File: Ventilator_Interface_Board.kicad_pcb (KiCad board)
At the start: 2 copper layers, 60 x 88.5 mm, 53 parts, among them J1 ROTARY CONTROLS, J3 ALARM, J4 LCD DISPLAY, J5 OPTICAL SWITCH, J6 HOME LIMIT SWITCH, P1 Power, P2 Analog, P3 Digital, P4 Digital, P5 CONN_01X01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

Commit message: Rev A - pre-release
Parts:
- removed J5: OPTICAL SWITCH, Ventilator:Molex_KK-254_1x05_P2.54mm_Horizontal
- removed J6: HOME LIMIT SWITCH, Ventilator:Molex_KK-254_1x06_P2.54mm_Horizontal
- removed REF**: KiCad-Logo2_6mm_SilkScreen, Symbol:KiCad-Logo2_6mm_SilkScreen
- removed REF**: OSHW-Logo2_14.6x12mm_SilkScreen, Symbol:OSHW-Logo2_14.6x12mm_SilkScreen
- removed U2: HSCDRRN100MDAA5, Ventilator:DIP-8_W13.08mm
- added C7: 1uF, Capacitor_SMD:C_0603_1608Metric, F.Cu at (155.3, 111.8)
- added C8: 470pF, Capacitor_SMD:C_0603_1608Metric, F.Cu at (160.7, 104.9)
- added J2: Conn_01x08, Ventilator:PhoenixContact_PTSA_1,5_8-3_5-Z_1x08_P3.50mm_Vertical, F.Cu at (149.3, 68.4)
- added R10: 330R, Resistor_SMD:R_0603_1608Metric, F.Cu at (157.0, 128.6)
- added R9: 10K, Resistor_SMD:R_0603_1608Metric, F.Cu at (151.0, 127.6)
- J1: value ROTARY CONTROLS -> Conn_01x08; footprint Ventilator:Molex_KK-254_1x08_P2.54mm_Horizontal -> Ventilator:PhoenixContact_PTSA_1,5_8-3_5-Z_1x08_P3.50mm_Vertical
- J3: value ALARM -> Conn_01x08; footprint Ventilator:Molex_KK-254_1x04_P2.54mm_Horizontal -> Ventilator:PhoenixContact_PTSA_1,5_8-3_5-Z_1x08_P3.50mm_Vertical
- J4: value LCD DISPLAY -> Conn_01x08; footprint Ventilator:Molex_KK-254_1x12_P2.54mm_Horizontal -> Ventilator:PhoenixContact_PTSA_1,5_8-3_5-Z_1x08_P3.50mm_Vertical
- R3: value 10K -> DNF
- R7: value 330R -> 0R
- U1: value HSCMRRN100MDAA5 -> MP3V5004GP; footprint Ventilator:SMT-8W_7.5x8.8mm_P2.54mm -> Ventilator:SOP_16.8x7.62mm_P2.54mm
- moved J4 82.5 mm to (126.3, 132.5), turned to 0 degrees
- moved J1 64.9 mm to (180.3, 68.4), turned to 180 degrees
- moved J3 64.0 mm to (157.1, 132.5), turned to 0 degrees
- moved R2 22.0 mm to (133.3, 127.6), turned to 90 degrees
- moved R4 21.6 mm to (130.3, 127.6), turned to 90 degrees
- moved R3 20.6 mm to (151.6, 111.7)
- moved C5 20.4 mm to (179.1, 128.5), turned to 180 degrees
- moved R5 15.7 mm to (147.4, 127.6), turned to 90 degrees
- moved R7 15.1 mm to (149.6, 111.7), turned to 270 degrees
- moved C2 13.0 mm to (136.1, 127.5), turned to 270 degrees
- moved R8 9.56 mm to (139.6, 128.1), turned to 180 degrees
- moved C4 3.89 mm to (155.3, 110.0), turned to 180 degrees
- moved R1 3.01 mm to (133.9, 72.4), turned to 0 degrees
- moved R6 0.69 mm to (152.4, 72.7), turned to 0 degrees
- moved U1 0.30 mm to (155.3, 98.7)
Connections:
- C4 pad 2: +5V -> Net-(C4-Pad2)
- J1 pad 1: +5V -> GND
- J1 pad 2: /TIDAL_VOLUME -> +5V
- J1 pad 3: /BPM -> +5V
- J1 pad 4: /IF_RATE -> /LCD_RS
- J1 pad 5: /MAX_PRESSURE -> GND
- J1 pad 6: GND -> /LCD_EN
- J1 pad 7: (no net) -> /LCD_D4
- J1 pad 8: (no net) -> /LCD_D5
- J3 pad 1: /BUZZER_LED -> Net-(J3-Pad1)
- J3 pad 2: GND -> +5V
- J3 pad 3: /BUZZER_LED -> /TIDAL_VOLUME
- J3 pad 4: Net-(J3-Pad4) -> /BPM
- J4 pad 2: +5V -> Net-(J4-Pad2)
- J4 pad 3: +5V -> /OPTICAL_SW
- J4 pad 4: /LCD_RS -> +5V
- J4 pad 5: GND -> Net-(J4-Pad5)
- J4 pad 6: /LCD_EN -> GND
- J4 pad 7: /LCD_D4 -> Net-(J4-Pad7)
- J4 pad 8: /LCD_D5 -> /HOME_LIMIT_SW
- R1 pad 1: Net-(J3-Pad4) -> Net-(J2-Pad8)
- R2 pad 1: +5V -> /OPTICAL_SW
- R2 pad 2: /OPTICAL_SW -> +5V
- R3 pad 1: +5V -> Net-(C4-Pad2)
- R3 pad 2: /HOME_LIMIT_SW -> +5V
- R4 pad 1: +5V -> Net-(J4-Pad2)
- R4 pad 2: Net-(J5-Pad4) -> +5V
- R5 pad 1: +5V -> Net-(J4-Pad7)
- R5 pad 2: Net-(J6-Pad4) -> +5V
- R6 pad 1: Net-(J4-Pad11) -> Net-(J2-Pad3)
- R7 pad 1: Net-(J5-Pad2) -> Net-(C4-Pad2)
- R7 pad 2: GND -> +3V3
- R8 pad 1: Net-(J6-Pad2) -> Net-(J4-Pad5)
- U1 pad 2: +5V -> Net-(C4-Pad2)
- U1 pad 3: /PRESSURE_SENSOR -> GND
- U1 pad 4: GND -> /PRESSURE_SENSOR
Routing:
- net +5V: track 164.7 -> 202.9 mm, vias 0 -> 2
- net /OPTICAL_SW: track 85.6 -> 108.0 mm
- net Net-(J2-Pad8): track 0.00 -> 15.8 mm
- net /LCD_D7: track 9.94 -> 22.8 mm
- net /HOME_LIMIT_SW: track 56.7 -> 44.2 mm, vias 0 -> 1
- net Net-(J2-Pad3): track 0.00 -> 11.2 mm
- net Net-(C4-Pad2): track 0.00 -> 10.00 mm
- net /MAX_PRESSURE: track 11.6 -> 21.5 mm
- net Net-(J4-Pad2): track 0.00 -> 9.32 mm
- net /BUZZER_LED: track 22.0 -> 31.1 mm
- net /BPM: track 9.73 -> 18.8 mm
- net +3V3: track 5.13 -> 13.4 mm
- net /LCD_D6: track 9.96 -> 17.8 mm, vias 0 -> 1
- net Net-(J6-Pad4): track 6.42 -> 0.00 mm
- net /PRESSURE_SENSOR: track 31.3 -> 26.1 mm
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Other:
- board size 60 x 88.5 mm -> 63 x 100 mm
- board text added: "+5V"
- board text added: "BPM"
- board text added: "BUZZ"
- board text added: "D4"
- board text added: "D5"
- board text added: "D6"
- board text added: "D7"
- board text added: "EN"
- board text added: "GND"
- board text added: "H_SW"
- board text added: "IF RT"
- board text added: "LED_A"
- board text added: "LED_K"
- board text added: "O_SW"
- board text added: "PRES."
- board text added: "P_UP"
- board text added: "RS"
- board text added: "TIDAL"

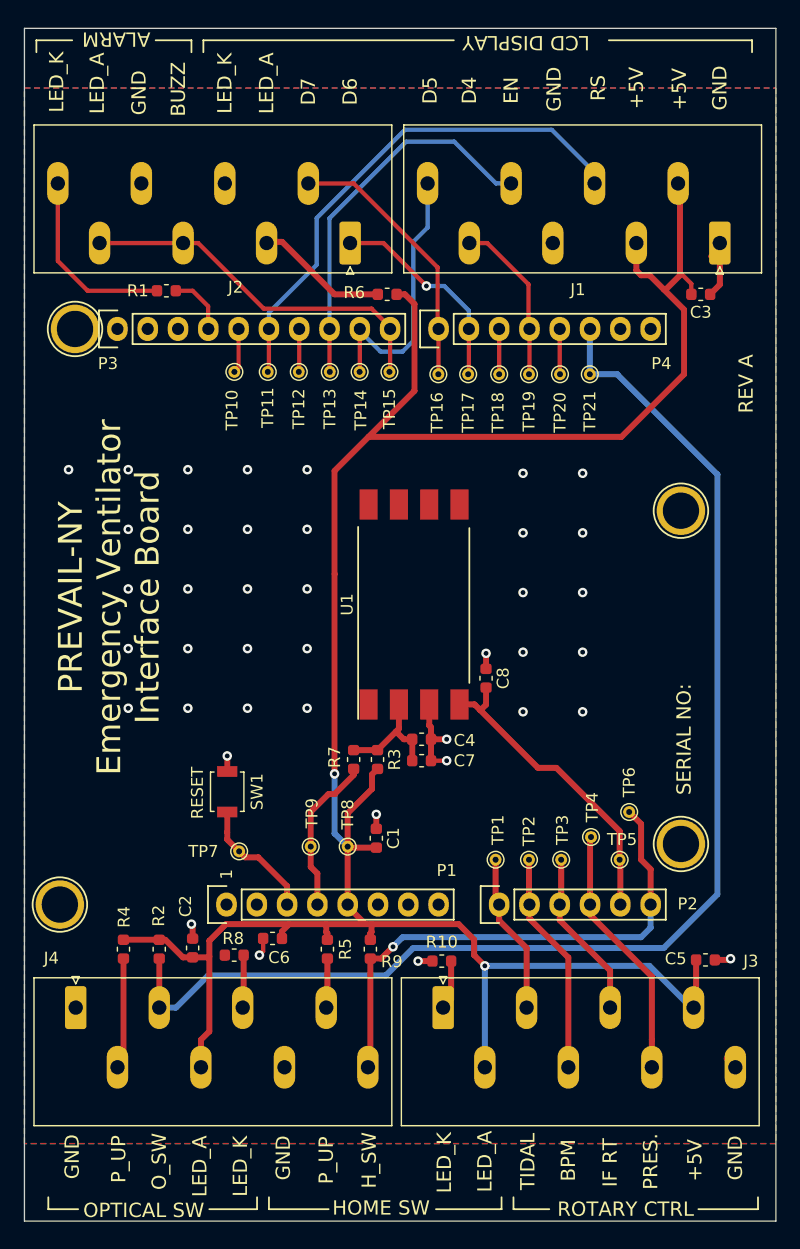
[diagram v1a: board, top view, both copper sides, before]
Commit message: minor changes to make design more flexible
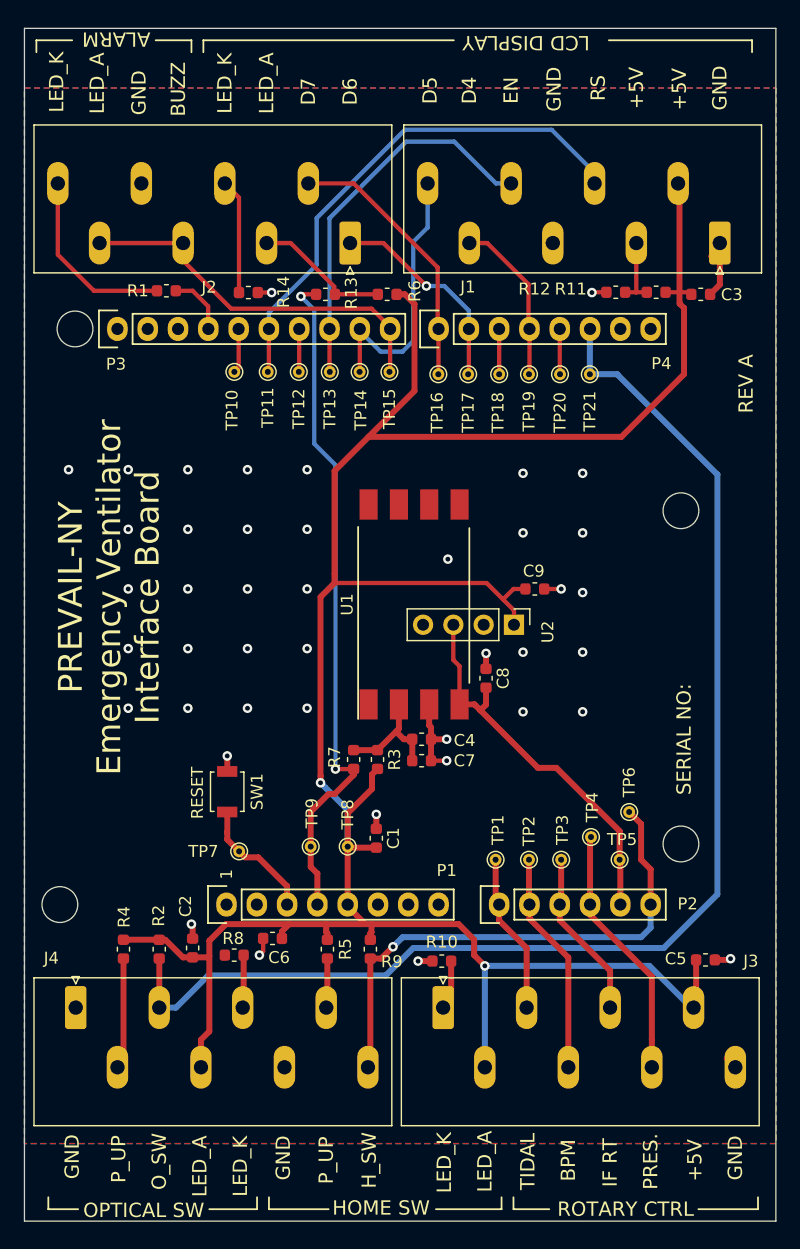
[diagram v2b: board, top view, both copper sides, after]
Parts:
- added C9: 100nF, Capacitor_SMD:C_0603_1608Metric, F.Cu at (164.8, 97.4)
- added R11: 10K, Resistor_SMD:R_0603_1608Metric, F.Cu at (175.0, 72.5)
- added R12: DNF, Resistor_SMD:R_0603_1608Metric, F.Cu at (171.6, 72.5)
- added R13: DNF, Resistor_SMD:R_0603_1608Metric, F.Cu at (147.2, 72.7)
- added R14: 0R, Resistor_SMD:R_0603_1608Metric, F.Cu at (140.8, 72.5)
- added U2: PSI-G-XX-MINI, Connector_PinHeader_2.54mm:PinHeader_1x04_P2.54mm_Vertical, F.Cu at (163.0, 100.4)
- P5, P6, P7, P8: footprint Socket_Arduino_Uno:Arduino_1pin -> MountingHole:MountingHole_3mm
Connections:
- J1 pad 3: +5V -> Net-(J1-Pad3)
- J2 pad 4: GND -> Net-(J2-Pad4)
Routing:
- net +3V3: track 13.4 -> 57.1 mm, vias 0 -> 2
- net +5V: track 202.9 -> 215.5 mm
- net Net-(J2-Pad4): track 0.00 -> 9.64 mm
- net /PRESSURE_SENSOR: track 26.1 -> 33.0 mm
- net Net-(J1-Pad3): track 0.00 -> 5.95 mm
- net GND: track 27.3 -> 31.1 mm, vias 39 -> 42
- net /BUZZER_LED: track 31.1 -> 31.9 mm
